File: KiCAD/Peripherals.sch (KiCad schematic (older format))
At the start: 0 parts

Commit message: completed 5V buck schematic and setup
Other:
- note added: "3 state leds"
- note added: "Motor Driver"
- note added: "TX module"
- note added: "Thermocouples and conn"
- note added: "button"
- note added: "uSD"
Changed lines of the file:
@@
 LIBS:contrib
 LIBS:valves
+LIBS:TPS565208
 LIBS:OBC-PDB-cache
 EELAYER 25 0
@@
 $Descr A4 11693 8268
 encoding utf-8
-Sheet 1 1
+Sheet 5 6
 Title ""
 Date ""
@@
 Comment4 ""
 $EndDescr
+Text Notes 2050 4900 0    118  ~ 0
+Motor Driver
+Text Notes 6800 4850 0    118  ~ 0
+Thermocouples and conn
+Text Notes 2050 6600 0    118  ~ 0
+uSD
+Text Notes 7000 1900 0    118  ~ 0
+TX module
+Text Notes 2050 2900 0    118  ~ 0
+button
+Text Notes 1950 2250 0    118  ~ 0
+3 state leds
 $EndSCHEMATC

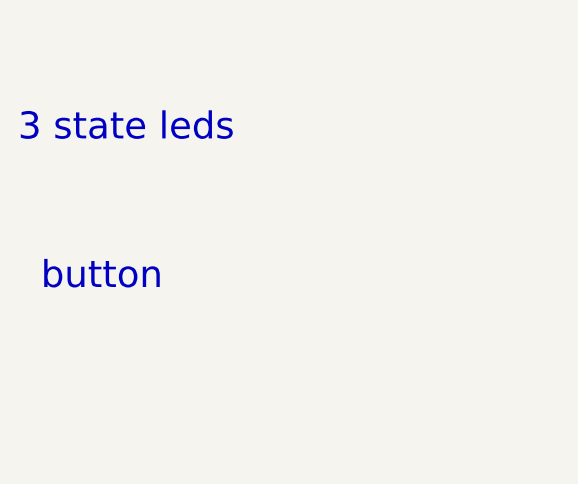
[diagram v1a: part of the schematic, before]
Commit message: µC ATMEGA2560 added and pins labeled, w/ supp components
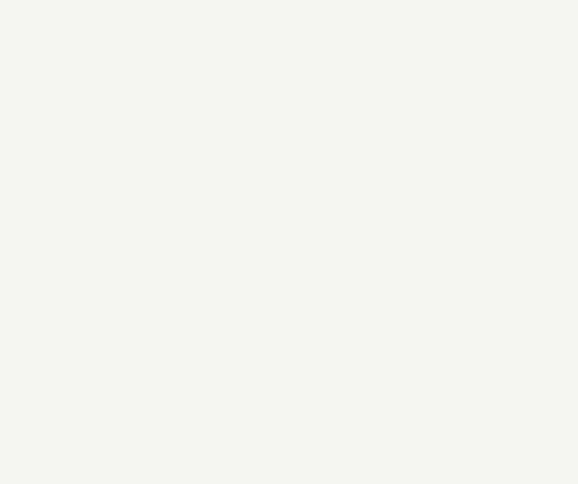
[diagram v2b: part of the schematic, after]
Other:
- note removed: "3 state leds"
- note removed: "button"
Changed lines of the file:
@@
 LIBS:valves
 LIBS:TPS565208
+LIBS:Switch
 LIBS:OBC-PDB-cache
 EELAYER 25 0
@@
 Text Notes 7000 1900 0    118  ~ 0
 TX module
-Text Notes 2050 2900 0    118  ~ 0
-button
-Text Notes 1950 2250 0    118  ~ 0
-3 state leds
 $EndSCHEMATC

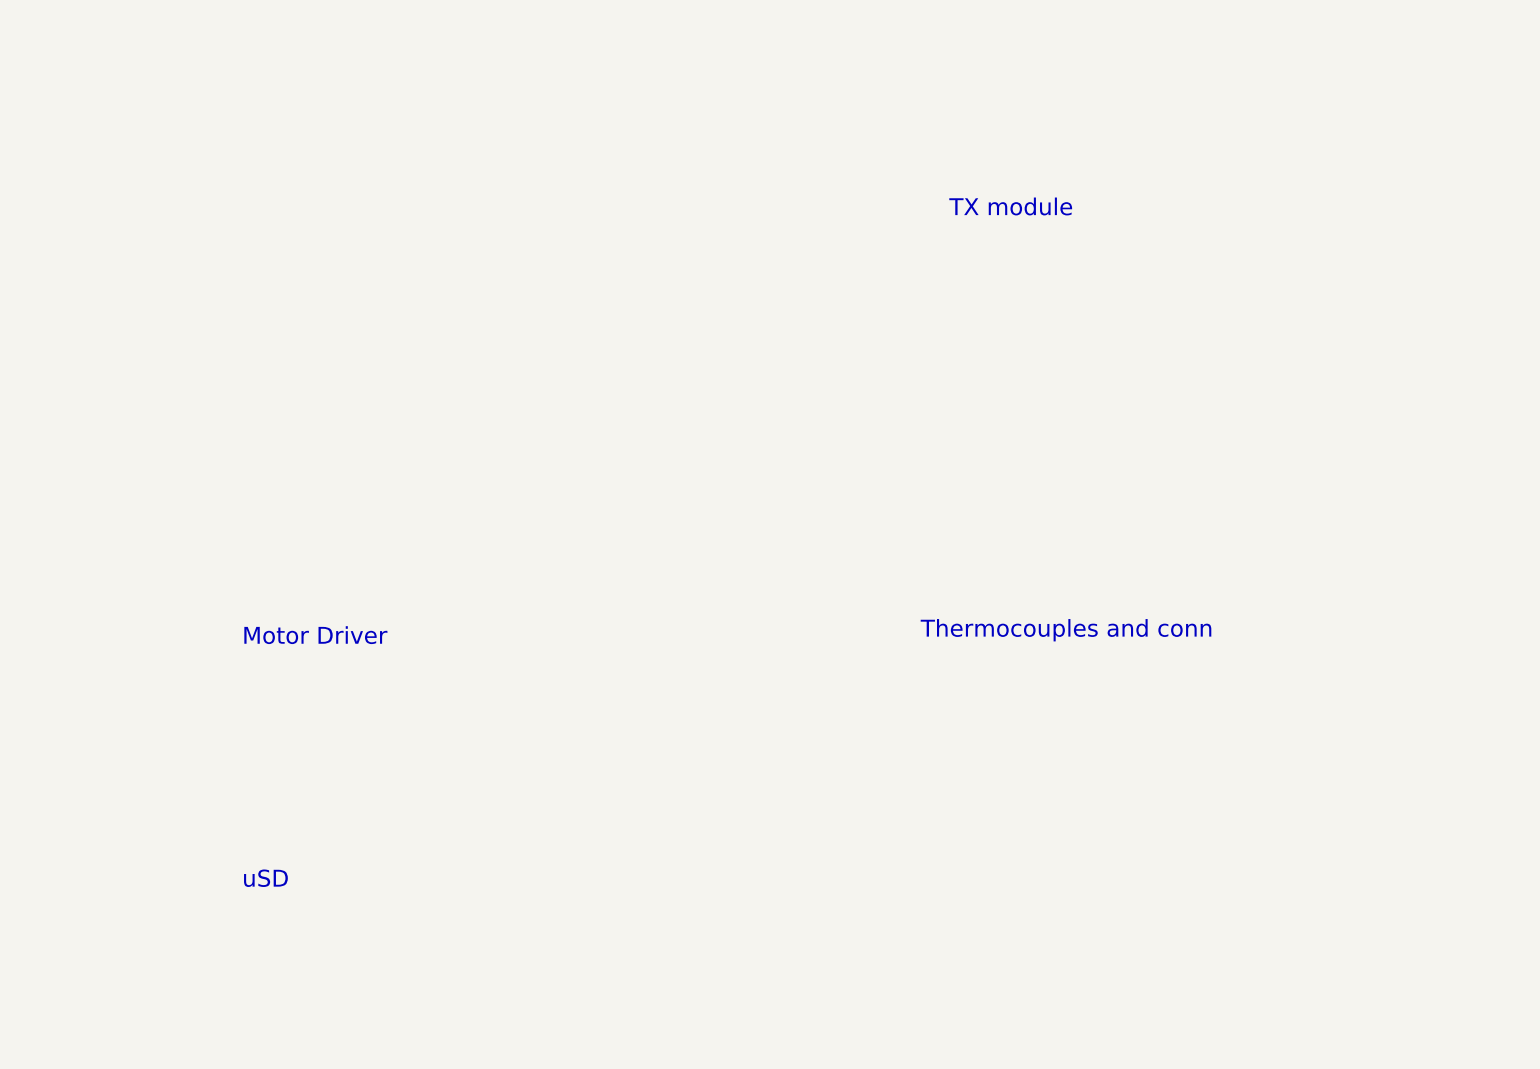
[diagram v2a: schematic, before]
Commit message: Schematic small fix
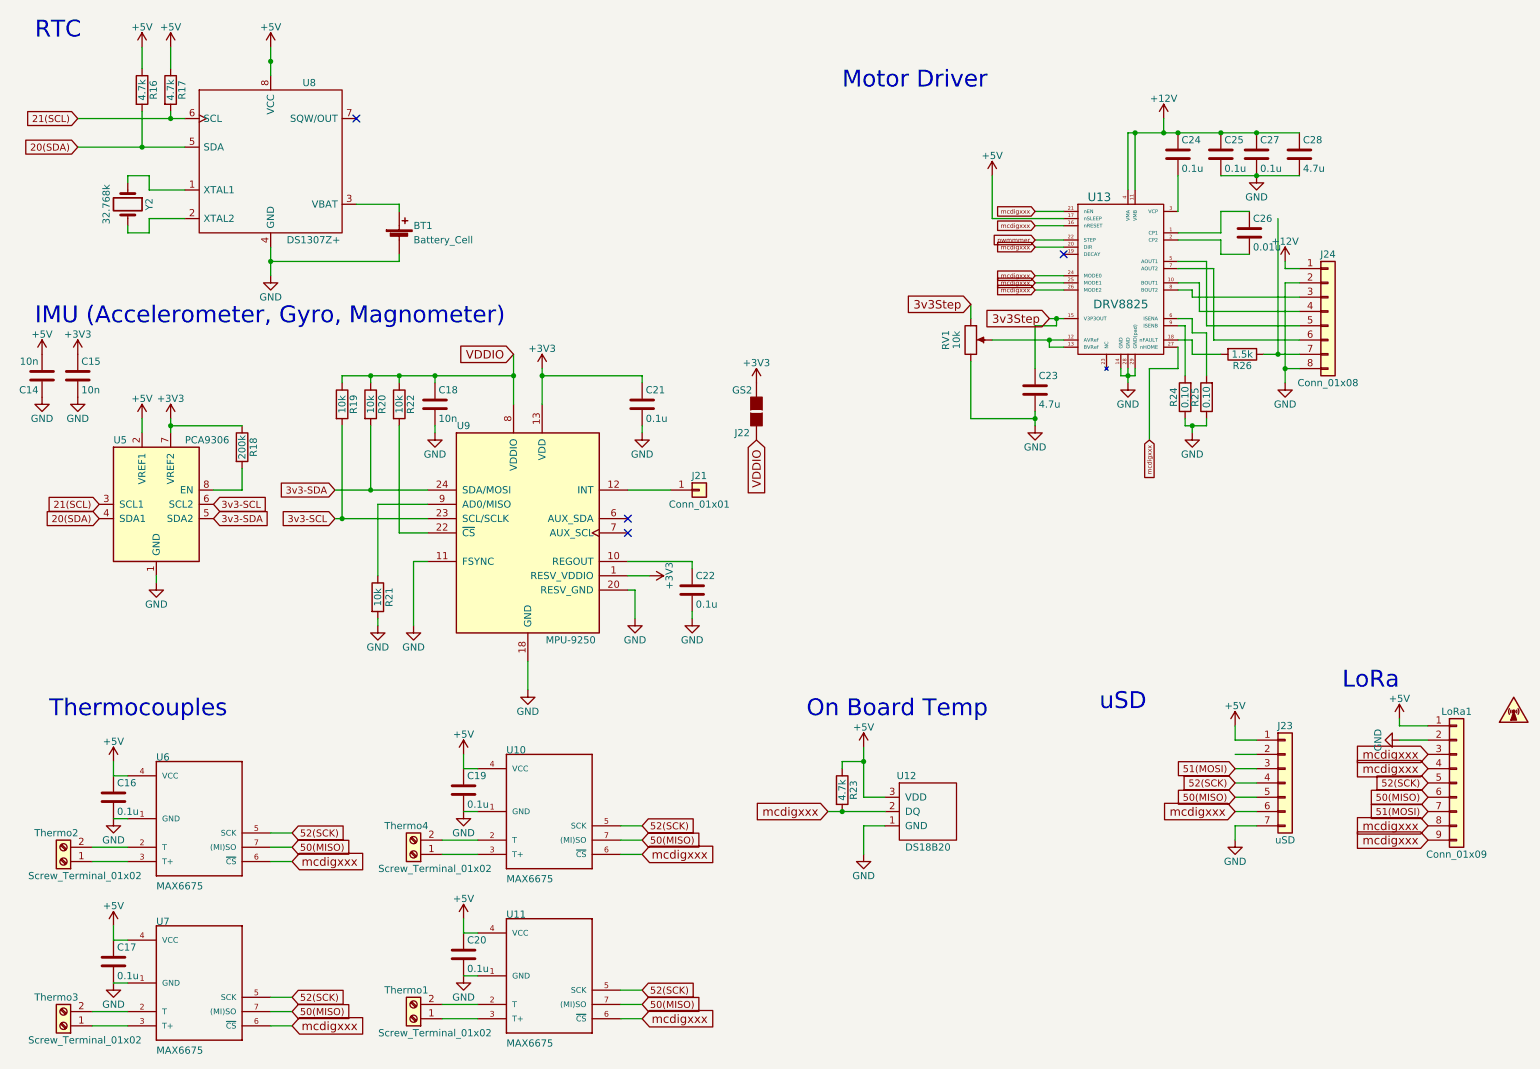
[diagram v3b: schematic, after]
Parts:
- added BT1: Battery_Cell, Battery_Holders:Keystone_1058_1x2032-CoinCell, symbol Battery_Cell
- added C14, C15, C18: 10n, Capacitors_SMD:C_0805, symbol C
- added C16, C17, C19, C20, C21, C22, C24, C25, C27: 0.1u, Capacitors_SMD:C_0805, symbol C
- added C23, C28: 4.7u, Capacitors_SMD:C_0805, symbol C
- added C26: 0.01u, Capacitors_SMD:C_0805, symbol C
- added J21: Conn_01x01, Pin_Headers:Pin_Header_Straight_1x01_Pitch2.54mm, symbol Conn_01x01
- added J22: GS2, Connectors:GS2, symbol GS2
- added J23: uSD, Pin_Headers:Pin_Header_Straight_1x07_Pitch2.54mm, symbol Conn_01x07
- added J24: Conn_01x08, Connectors_JST:JST_XH_B08B-XH-A_08x2.50mm_Straight, symbol Conn_01x08
- added LoRa1: Conn_01x09, Pin_Headers:Pin_Header_Straight_1x09_Pitch2.54mm, symbol Conn_01x09
- added R16, R17, R23: 4.7k, Resistors_SMD:R_0805, symbol R
- added R18: 200k, Resistors_SMD:R_0805, symbol R
- added R19, R20, R21, R22: 10k, Resistors_SMD:R_0805, symbol R
- added R24, R25: 0.10, Resistors_SMD:R_0805, symbol R
- added R26: 1.5k, Resistors_SMD:R_0805, symbol R
- added RV1: 10k, Pin_Headers:Pin_Header_Straight_1x03_Pitch2.54mm, symbol POT
- added Thermo1, Thermo2, Thermo3, Thermo4: Screw_Terminal_01x02, TerminalBlock:TerminalBlock_bornier-2_P5.08mm, symbol Screw_Terminal_01x02
- added U10, U11, U6, U7: MAX6675, Housings_SOIC:SOIC-8_3.9x4.9mm_Pitch1.27mm, symbol MAX6675
- added U12: DS18B20, TO_SOT_Packages_THT:TO-92_Inline_Narrow_Oval, symbol DS18B20
- added U13: DRV8825, Housings_SSOP:HTSSOP-20-1EP_4.4x6.5mm_Pitch0.65mm_ThermalPad, symbol DRV8825
- added U5: PCA9306, symbol PCA9306
- added U8: DS1307Z+, Housings_SOIC:SOIC-8_3.9x4.9mm_Pitch1.27mm, symbol DS1307Z+
- added U9: MPU-9250, 10k, symbol MPU-9250
- added Y2: 32.768k, symbol Crystal
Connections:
- new net: BT1.1 (+), U8.3 (VBAT)
- new net: U8.1 (XTAL1), Y2.1
- new net: U8.2 (XTAL2), Y2.2
- new net: C22.1, U9.10 (REGOUT)
- new net: J21.1 (Pin_1), U9.12 (INT)
- new net: R22.2, U9.22 (~CS)
- new net: R21.1, U9.9 (AD0/MISO)
- new net: C26.1, U13.1 (CP1)
- new net: J24.4 (Pin_4), U13.10 (BOUT1)
- new net: RV1.2, U13.12 (AVRef), U13.13 (BVRef)
- new net: R26.2, U13.18 (nFAULT)
- new net: C26.2, U13.2 (CP2)
- new net: C24.2, U13.3 (VCP)
- new net: J24.5 (Pin_5), U13.5 (AOUT1)
- new net: R25.2, U13.6 (ISENA)
- new net: J24.6 (Pin_6), U13.7 (AOUT2)
- new net: J24.3 (Pin_3), U13.8 (BOUT2)
- new net: R24.2, U13.9 (ISENB)
- new net: R18.2, U5.8 (EN)
- new net: Thermo1.2 (Pin_2), U11.2 (T)
- new net: Thermo1.1 (Pin_1), U11.3 (T+)
- new net: Thermo4.2 (Pin_2), U10.2 (T)
- new net: Thermo4.1 (Pin_1), U10.3 (T+)
- new net: Thermo3.2 (Pin_2), U7.2 (T)
- new net: Thermo3.1 (Pin_1), U7.3 (T+)
- new net: Thermo2.2 (Pin_2), U6.2 (T)
- new net: Thermo2.1 (Pin_1), U6.3 (T+)
- new net: J24.7 (Pin_7), R26.1
- new net +12V: C24.1, C25.1, C27.1, C28.1, J24.1 (Pin_1), U13.11 (VMB), U13.4 (VMA)
- new net +3V3: C15.1, C21.1, J22.2 (G2), R18.1, U5.7 (VREF2), U9.1 (RESV_VDDIO), U9.13 (VDD)
- new net +5V: C14.2, C16.1, C17.1, C19.1, C20.1, J23.1 (Pin_1), LoRa1.1 (Pin_1), R16.1, R17.1, R23.1, U10.4 (VCC), U11.4 (VCC), U12.3 (VDD), U13.17 (nSLEEP), U5.2 (VREF1), U6.4 (VCC), U7.4 (VCC), U8.8 (VCC)
- new net 20(SDA): R16.2, U5.4 (SDA1), U8.5 (SDA)
- new net 21(SCL): R17.2, U5.3 (SCL1), U8.6 (SCL)
- new net 3v3-SCL: R19.2, U5.6 (SCL2), U9.23 (SCL/SCLK)
- new net 3v3-SDA: R20.2, U5.5 (SDA2), U9.24 (SDA/MOSI)
- new net 3v3Step: C23.1, RV1.1, U13.15 (V3P3OUT)
- new net 50(MISO): J23.5 (Pin_5), LoRa1.6 (Pin_6), U10.7 ((MI)SO), U11.7 ((MI)SO), U6.7 ((MI)SO), U7.7 ((MI)SO)
- new net 51(MOSI): J23.3 (Pin_3), LoRa1.7 (Pin_7)
- new net 52(SCK): J23.4 (Pin_4), LoRa1.5 (Pin_5), U10.5 (SCK), U11.5 (SCK), U6.5 (SCK), U7.5 (SCK)
- new net GND: BT1.2 (-), C14.1, C15.2, C16.2, C17.2, C18.2, C19.2, C20.2, C21.2, C22.2, C23.2, C25.2, C27.2, C28.2, J23.7 (Pin_7), J24.2 (Pin_2), J24.8 (Pin_8), LoRa1.2 (Pin_2), R21.2, R24.1, R25.1, RV1.3, U10.1 (GND), U11.1 (GND), U12.1 (GND), U13.14 (GND), U13.28 (GND), U13.29 (GND(pad)), U5.1 (GND), U6.1 (GND), U7.1 (GND), U8.4 (GND), U9.11 (FSYNC), U9.18 (GND), U9.20 (RESV_GND)
- new net VDDIO: C18.1, J22.1 (G1), R19.1, R20.1, R22.1, U9.8 (VDDIO)
- new net mcdigxxx: J23.6 (Pin_6), LoRa1.3 (Pin_3), LoRa1.4 (Pin_4), LoRa1.8 (Pin_8), LoRa1.9 (Pin_9), R23.2, U10.6 (~CS~), U11.6 (~CS~), U12.2 (DQ), U13.16 (nRESET), U13.20 (DIR), U13.21 (nEN), U13.24 (MODE0), U13.25 (MODE1), U13.26 (MODE2), U13.27 (nHOME), U6.6 (~CS~), U7.6 (~CS~)
- new net pwmmmer: U13.22 (STEP)
- no-connect marks 0 -> 4
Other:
- note added: "IMU (Accelerometer, Gyro, Magnometer)"
- note added: "LoRa\n"
- note added: "On Board Temp"
- note added: "RTC"
- note added: "Thermocouples"
- note removed: "TX module"
- note removed: "Thermocouples and conn"

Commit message: transfer for mechanical step
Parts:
- U13: footprint Housings_SSOP:HTSSOP-20-1EP_4.4x6.5mm_Pitch0.65mm_ThermalPad -> Housings_SSOP:HTSSOP-32_6.1x11mm_Pitch0.65mm_ThermalPad
- U5: footprint (none) -> Housings_SSOP:VSSOP-8_2.3x2mm_Pitch0.5mm
- U9: footprint 10k -> Housings_DFN_QFN:QFN-24-1EP_3x3mm_Pitch0.4mm
- Y2: footprint (none) -> Crystals:Crystal_C26-LF_d2.1mm_l6.5mm_Horizontal
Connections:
- net 13(PWM): now reaches J23.2 (Pin_2)
- removed net mcdigxxx: J23.6 (Pin_6), LoRa1.3 (Pin_3), LoRa1.4 (Pin_4), LoRa1.8 (Pin_8), LoRa1.9 (Pin_9), R23.2, U10.6 (~CS~), U11.6 (~CS~), U12.2 (DQ), U13.16 (nRESET), U13.20 (DIR), U13.21 (nEN), U13.24 (MODE0), U13.25 (MODE1), U13.26 (MODE2), U13.27 (nHOME), U6.6 (~CS~), U7.6 (~CS~)
- net pwmmmer renamed 5(PWM)
- new net 12(PWM): J23.6 (Pin_6)
- new net 24: U13.16 (nRESET)
- new net 25: U13.20 (DIR)
- new net 26: U13.21 (nEN)
- new net 27: U13.24 (MODE0)
- new net 28: U13.25 (MODE1)
- new net 29: U13.26 (MODE2)
- new net 39: U13.27 (nHOME)
- new net 42: U11.6 (~CS~)
- new net 43: U6.6 (~CS~)
- new net 44(PWM): U7.6 (~CS~)
- new net 45(PWM): U10.6 (~CS~)
- new net A8: R23.2, U12.2 (DQ)
